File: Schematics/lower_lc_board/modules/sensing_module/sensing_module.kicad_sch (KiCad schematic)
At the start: 21 parts, among them J4 HALL-1, J5 HALL-2, Q3 2N7002, U11 SI2301CDS-T1-GE3, U9 ADC_ADS131M04IPWR

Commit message: organizational work
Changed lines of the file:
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@@
 	(text "place near sensor VCC pin"
 		(exclude_from_sim no)
-		(at 54.102 169.926 0)
+		(at 49.276 170.18 0)
 		(effects
 			(font

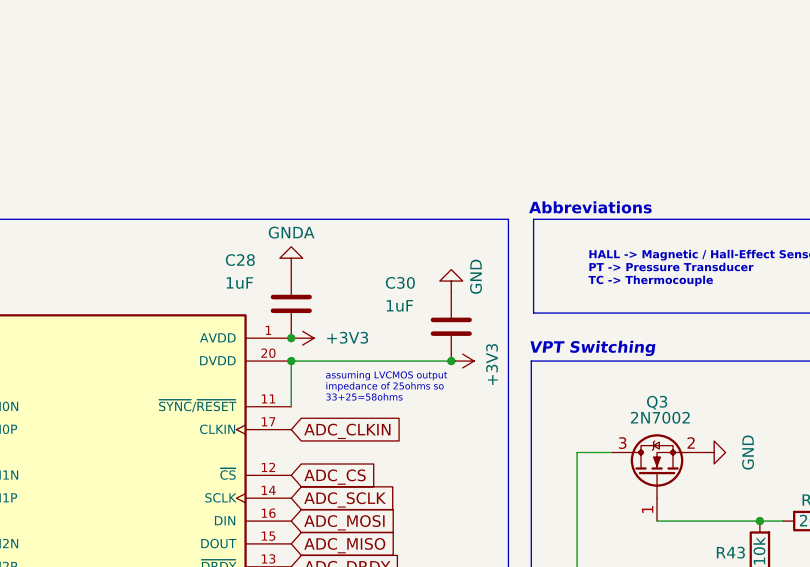
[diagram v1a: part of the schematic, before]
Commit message: more organizational work, add shared footprint, model, symbol dirs and clean up individuals
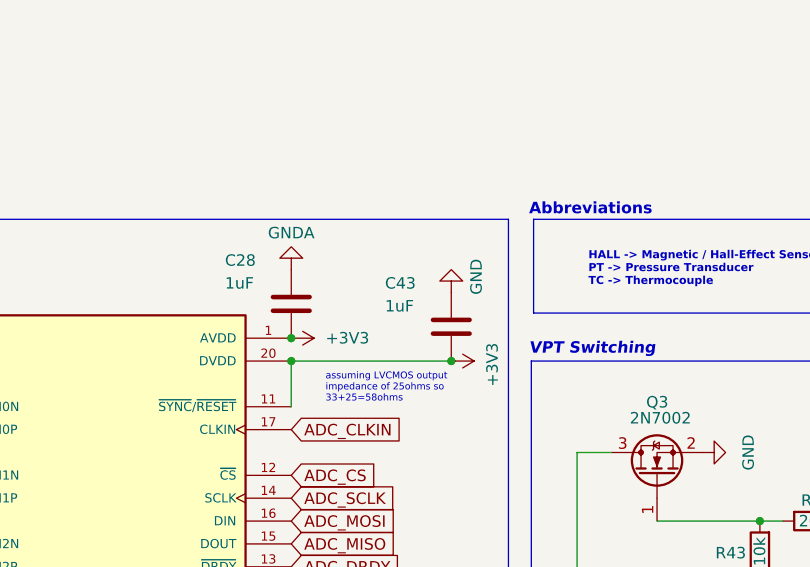
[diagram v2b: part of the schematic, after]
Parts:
- J4, J5: footprint S04B_PASK_2:CONN4_S04B-PASK_JST -> B04B_PASK_JST:CONN_B04B-PASK_JST
- renumbered C30 to C43
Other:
- title: Lower Board Sensing Module -> HYDRA | Sensing Circuitry
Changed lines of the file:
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@@
 	(paper "A4")
 	(title_block
-		(title "Lower Board Sensing Module")
-		(rev "B")
+		(title "HYDRA | Sensing Circuitry")
+		(rev "2")
 		(company "Queen's Rocket Engineering Team")
 		(comment 1 "Jeevan Sanchez")
@@
 			)
 		)
-		(property "Datasheet" "${KIPRJMOD}/../../Datasheets/NMOSFET-NDS7002A-D.PDF"
+		(property "Datasheet" "${KIPRJMOD}/../../Documentation/nmosfet_2N7002_DS.PDF"
 			(at 227.33 54.61 0)
 			(effects
@@
 			)
 		)
-		(property "Footprint" "S04B_PASK_2:CONN4_S04B-PASK_JST"
+		(property "Footprint" "B04B_PASK_JST:CONN_B04B-PASK_JST"
 			(at 49.53 154.94 0)
 			(effects
@@
 			)
 		)
-		(property "Datasheet" "${KIPRJMOD}/../../Datasheets/CONN-530470460.pdf"
+		(property "Datasheet" ""
 			(at 49.53 154.94 0)
 			(effects
@@
 		(on_board yes)
 		(dnp no)
-		(property "Reference" "C30"
+		(property "Reference" "C43"
 			(at 193.294 38.354 0)
 			(effects
@@
 			(project "lower_lc_board"
 				(path "/d63798c4-e363-437e-9012-e4aff32e6642/c6419db7-28a9-4bfa-8244-fc88166c795c"
-					(reference "C30")
+					(reference "C43")
 					(unit 1)
 				)
@@
 			)
 		)
-		(property "Datasheet" "https://www.vishay.com/doc?68741"
+		(property "Datasheet" "${KIPRJMOD}/../../Documentation/pmosfet_si2301cd_DS.pdf"
 			(at 229.87 80.01 0)
 			(effects
@@
 			)
 		)
-		(property "Footprint" "S04B_PASK_2:CONN4_S04B-PASK_JST"
+		(property "Footprint" "B04B_PASK_JST:CONN_B04B-PASK_JST"
 			(at 49.53 115.57 0)
 			(effects
@@
 			)
 		)
-		(property "Datasheet" "${KIPRJMOD}/../../Datasheets/CONN-530470460.pdf"
+		(property "Datasheet" ""
 			(at 49.53 115.57 0)
 			(effects
@@
 			)
 		)
-		(property "Datasheet" "${KIPRJMOD}/../../Datasheets/ADC-ads131m04.pdf"
+		(property "Datasheet" "${KIPRJMOD}/../../Documentation/ADC_ads131m04_DS.pdf"
 			(at 162.56 64.77 0)
 			(effects

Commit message: routing work
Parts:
- added R49: 10k, Resistor_SMD:R_0402_1005Metric, symbol Device:R
- C23, C33: JLCPCB (none) -> C49678
- J4, J5: footprint B04B_PASK_JST:CONN_B04B-PASK_JST -> S04B_PASK_2-P:CONN4_S04B-PASK_JST
- R22, R23: JLCPCB (none) -> C25744
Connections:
- net +3V3: now also R49.1
- net ADC_CS: now also R49.2
- net ADC_MISO renamed SPI_MISO
- net ADC_MOSI renamed SPI_MOSI
- net ADC_SCLK renamed SPI_SCLK
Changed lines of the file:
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@@
 		)
 	)
-	(global_label "ADC_DRDY"
+	(global_label "SPI_MISO"
 		(shape input)
-		(at 182.88 69.85 0)
+		(at 182.88 67.31 0)
 		(fields_autoplaced yes)
 		(effects
@@
 		)
 		(property "Intersheetrefs" "${INTERSHEET_REFS}"
-			(at 195.36 69.85 0)
+			(at 194.5133 67.31 0)
 			(effects
 				(font
@@
 		)
 	)
-	(global_label "HALL_SCL"
+	(global_label "ADC_DRDY"
 		(shape input)
-		(at 91.44 139.7 180)
+		(at 182.88 69.85 0)
 		(fields_autoplaced yes)
 		(effects
@@
 				(size 1.27 1.27)
 			)
-			(justify right)
+			(justify left)
 		)
 		(property "Intersheetrefs" "${INTERSHEET_REFS}"
-			(at 79.5043 139.7 0)
+			(at 195.36 69.85 0)
 			(effects
 				(font
 					(size 1.27 1.27)
 				)
-				(justify right)
+				(justify left)
 				(hide yes)
 			)
 		)
 	)
-	(global_label "ADC_CS"
+	(global_label "HALL_SCL"
 		(shape input)
-		(at 182.88 59.69 0)
+		(at 91.44 139.7 180)
 		(fields_autoplaced yes)
 		(effects
@@
 				(size 1.27 1.27)
 			)
-			(justify left)
+			(justify right)
 		)
 		(property "Intersheetrefs" "${INTERSHEET_REFS}"
-			(at 192.9409 59.69 0)
+			(at 79.5043 139.7 0)
 			(effects
 				(font
 					(size 1.27 1.27)
 				)
-				(justify left)
+				(justify right)
 				(hide yes)
 			)
 		)
 	)
-	(global_label "ADC_SCLK"
+	(global_label "ADC_CS"
 		(shape input)
-		(at 182.88 62.23 0)
+		(at 182.88 59.69 0)
 		(fields_autoplaced yes)
 		(effects
@@
 		)
 		(property "Intersheetrefs" "${INTERSHEET_REFS}"
-			(at 195.239 62.23 0)
+			(at 192.9409 59.69 0)
 			(effects
 				(font
@@
 		)
 	)
-	(global_label "ADC_MOSI"
+	(global_label "ADC_CLKIN"
 		(shape input)
-		(at 182.88 64.77 0)
+		(at 182.88 54.61 0)
 		(fields_autoplaced yes)
 		(effects
@@
 		)
 		(property "Intersheetrefs" "${INTERSHEET_REFS}"
-			(at 195.0576 64.77 0)
+			(at 195.9648 54.61 0)
 			(effects
 				(font
@@
 		)
 	)
-	(global_label "ADC_CLKIN"
+	(global_label "ADC_CS"
 		(shape input)
-		(at 182.88 54.61 0)
+		(at 203.2 78.74 90)
 		(fields_autoplaced yes)
 		(effects
@@
 		)
 		(property "Intersheetrefs" "${INTERSHEET_REFS}"
-			(at 195.9648 54.61 0)
+			(at 203.2 68.6791 90)
 			(effects
 				(font
@@
 		)
 	)
-	(global_label "ADC_MISO"
+	(global_label "SPI_SCLK"
 		(shape input)
-		(at 182.88 67.31 0)
+		(at 182.88 62.23 0)
 		(fields_autoplaced yes)
 		(effects
@@
 		)
 		(property "Intersheetrefs" "${INTERSHEET_REFS}"
-			(at 195.0576 67.31 0)
+			(at 194.6947 62.23 0)
 			(effects
 				(font
@@
 		)
 	)
+	(global_label "SPI_MOSI"
+		(shape input)
+		(at 182.88 64.77 0)
+		(fields_autoplaced yes)
+		(effects
+			(font
+				(size 1.27 1.27)
+			)
+			(justify left)
+		)
+		(property "Intersheetrefs" "${INTERSHEET_REFS}"
+			(at 194.5133 64.77 0)
+			(effects
+				(font
+					(size 1.27 1.27)
+				)
+				(justify left)
+				(hide yes)
+			)
+		)
+	)
 	(symbol
 		(lib_id "Device:C")
@@
 			)
 		)
+		(property "JLCPCB" "C25744"
+			(at 228.6 73.66 0)
+			(effects
+				(font
+					(size 1.27 1.27)
+				)
+				(hide yes)
+			)
+		)
 		(pin "1"
 		)
@@
 			)
 		)
+		(property "JLCPCB" "C49678"
+			(at 45.72 170.18 0)
+			(effects
+				(font
+					(size 1.27 1.27)
+				)
+				(hide yes)
+			)
+		)
 		(pin "2"
 		)
@@
 			)
 		)
-		(property "Footprint" "B04B_PASK_JST:CONN_B04B-PASK_JST"
+		(property "Footprint" "S04B_PASK_2-P:CONN4_S04B-PASK_JST"
 			(at 49.53 154.94 0)
 			(effects
@@
 			)
 		)
+		(property "JLCPCB" "C49678"
+			(at 45.72 130.81 0)
+			(effects
+				(font
+					(size 1.27 1.27)
+				)
+				(hide yes)
+			)
+		)
 		(pin "2"
 		)
@@
 	)
 	(symbol
+		(lib_id "power:+3V3")
+		(at 203.2 86.36 180)
+		(unit 1)
+		(exclude_from_sim no)
+		(in_bom yes)
+		(on_board yes)
+		(dnp no)
+		(property "Reference" "#PWR0132"
+			(at 203.2 82.55 0)
+			(effects
+				(font
+					(size 1.27 1.27)
+				)
+				(hide yes)
+			)
+		)
+		(property "Value" "+3V3"
+			(at 203.2 90.424 0)
+			(effects
+				(font
+					(size 1.27 1.27)
+				)
+			)
+		)
+		(property "Footprint" ""
+			(at 203.2 86.36 0)
+			(effects
+				(font
+					(size 1.27 1.27)
+				)
+				(hide yes)
+			)
+		)
+		(property "Datasheet" ""
+			(at 203.2 86.36 0)
+			(effects
+				(font
+					(size 1.27 1.27)
+				)
+				(hide yes)
+			)
+		)
+		(property "Description" "Power symbol creates a global label with name \"+3V3\""
+			(at 203.2 86.36 0)
+			(effects
+				(font
+					(size 1.27 1.27)
+				)
+				(hide yes)
+			)
+		)
+		(pin "1"
+		)
+		(instances
+			(project "lower_lc_board"
+				(path "/d63798c4-e363-437e-9012-e4aff32e6642/c6419db7-28a9-4bfa-8244-fc88166c795c"
+					(reference "#PWR0132")
+					(unit 1)
+				)
+			)
+		)
+	)
+	(symbol
 		(lib_id "Device:C")
 		(at 186.69 74.93 90)
@@
 			)
 		)
-		(property "Footprint" "B04B_PASK_JST:CONN_B04B-PASK_JST"
+		(property "Footprint" "S04B_PASK_2-P:CONN4_S04B-PASK_JST"
 			(at 49.53 115.57 0)
 			(effects
@@
 	(symbol
 		(lib_id "Device:R")
+		(at 203.2 82.55 180)
+		(unit 1)
+		(exclude_from_sim no)
+		(in_bom yes)
+		(on_board yes)
+		(dnp no)
+		(property "Reference" "R49"
+			(at 200.406 86.868 0)
+			(effects
+				(font
+					(size 1.27 1.27)
+				)
+				(justify left)
+			)
+		)
+		(property "Value" "10k"
+			(at 200.406 84.328 0)
+			(effects
+				(font
+					(size 1.27 1.27)
+				)
+				(justify left)
+			)
+		)
+		(property "Footprint" "Resistor_SMD:R_0402_1005Metric"
+			(at 204.978 82.55 90)
+			(effects
+				(font
+					(size 1.27 1.27)
+				)
+				(hide yes)
+			)
+		)
+		(property "Datasheet" "~"
+			(at 203.2 82.55 0)
+			(effects
+				(font
+					(size 1.27 1.27)
+				)
+				(hide yes)
+			)
+		)
+		(property "Description" "Resistor"
+			(at 203.2 82.55 0)
+			(effects
+				(font
+					(size 1.27 1.27)
+				)
+				(hide yes)
+			)
+		)
+		(property "JLCPCB" "C25744"
+			(at 203.2 82.55 0)
+			(effects
+				(font
+					(size 1.27 1.27)
+				)
+				(hide yes)
+			)
+		)
+		(pin "1"
+		)
+		(pin "2"
+		)
+		(instances
+			(project "lower_lc_board"
+				(path "/d63798c4-e363-437e-9012-e4aff32e6642/c6419db7-28a9-4bfa-8244-fc88166c795c"
+					(reference "R49")
+					(unit 1)
+				)
+			)
+		)
+	)
+	(symbol
+		(lib_id "Device:R")
 		(at 234.95 68.58 180)
 		(unit 1)
@@
 			(at 218.44 73.66 0)
 			(effects
+				(font
+					(size 1.27 1.27)
+				)
+				(hide yes)
+			)
+		)
+		(property "JLCPCB" "C25744"
+			(at 218.44 73.66 0)
+			(effects

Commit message: routing work
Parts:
- added C56: 10nF, Capacitor_SMD:C_0603_1608Metric, symbol Device:C
- added R25: 10k, Resistor_SMD:R_0603_1608Metric, symbol Device:R
- added TH1: Thermistor, Resistor_SMD:R_0402_1005Metric, symbol Device:Thermistor
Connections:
- net +3V3: now also R25.2
- net GNDA: now also TH1.2; no longer U9.10 (AIN3P), U9.9 (AIN3N)
- net TEMP_SENSE: now also R25.1, TH1.1
- net TC_N_CLAMPED renamed TC_N_CLAMPED_1
- net TC_P_CLAMPED renamed TC_P_CLAMPED_1
- new net TC_N_CLAMPED_2: C56.1, U9.9 (AIN3N)
- new net TC_P_CLAMPED_2: C56.2, U9.10 (AIN3P)
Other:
- added sheet TC Conditoning + CJC1 (../../../shared_schematics/TC_module.kicad_sch)
- sheet TC Conditoning + CJC ports: added none; removed TMP-OUT
- note added: "place as close as possible to thermocouple input for CJC measuring accuracy"

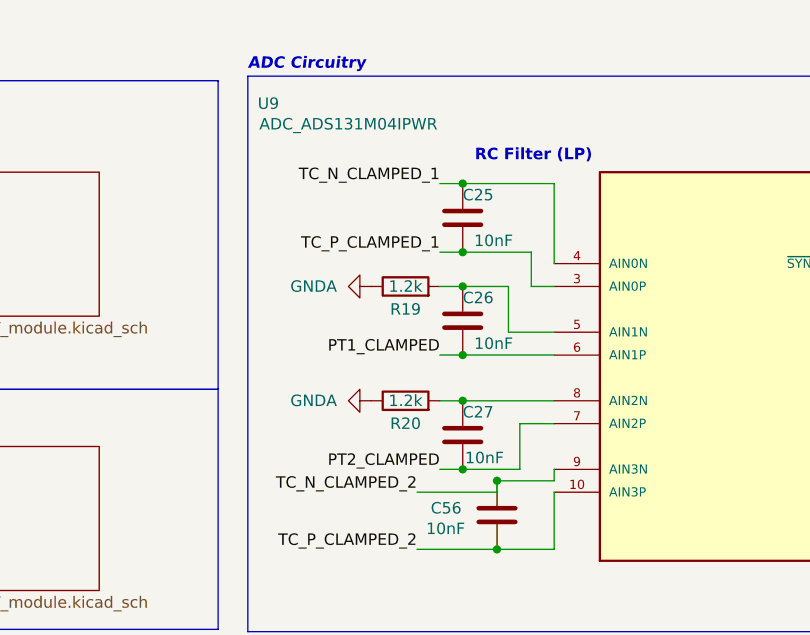
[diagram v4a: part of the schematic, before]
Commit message: ADC routing
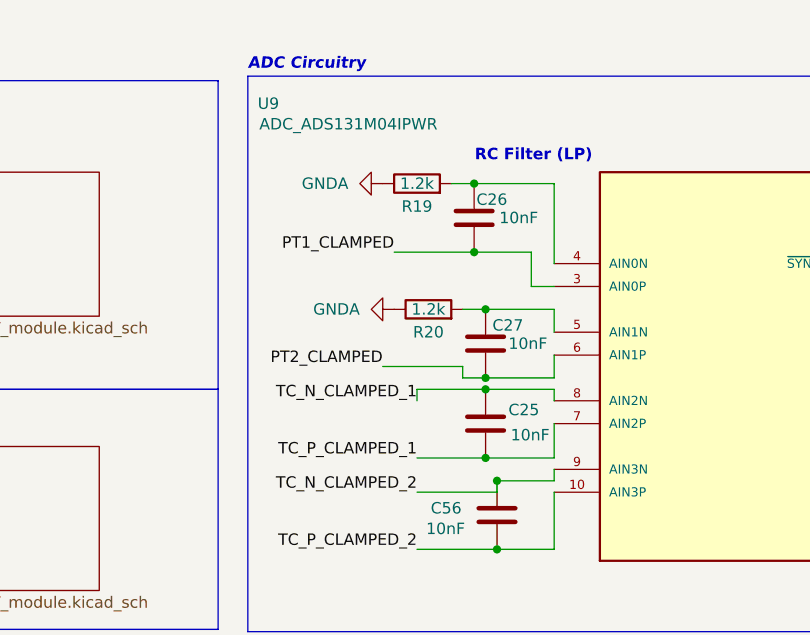
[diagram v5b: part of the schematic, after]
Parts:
- C29: footprint Capacitor_SMD:C_0805_2012Metric -> Capacitor_SMD:C_0402_1005Metric
- R19, R20: footprint Resistor_SMD:R_0603_1608Metric -> Resistor_SMD:R_0402_1005Metric
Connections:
- net PT1_CLAMPED: now also U9.3 (AIN0P); no longer U9.6 (AIN1P)
- net PT2_CLAMPED: now also U9.6 (AIN1P); no longer U9.7 (AIN2P)
- net TC_N_CLAMPED_1: now also U9.8 (AIN2N); no longer U9.4 (AIN0N)
- net TC_P_CLAMPED_1: now also U9.7 (AIN2P); no longer U9.3 (AIN0P)
- net at C26.1, R19.2: now also U9.4 (AIN0N); no longer U9.5 (AIN1N)
- net at C27.1, R20.2: now also U9.5 (AIN1N); no longer U9.8 (AIN2N)
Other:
- moved on the sheet: C25, C26, C27, R19, R20

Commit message: routing work
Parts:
- added C35: 10uF, Capacitor_SMD:C_1206_3216Metric, symbol Device:C
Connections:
- net GND: no longer Q3.2 (S), R43.1
- net GNDA: now also Q3.2 (S), R43.1, C35.2
- net VPT: now also C35.1
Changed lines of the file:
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@@
 	(wire
 		(pts
+			(xy 100.33 39.37) (xy 100.33 40.64)
+		)
+		(stroke
+			(width 0)
+			(type default)
+		)
+	)
+	(wire
+		(pts
 			(xy 223.52 116.84) (xy 223.52 118.11)
 		)
@@
 		)
 	)
+	(label "VPT"
+		(at 100.33 39.37 180)
+		(fields_autoplaced yes)
+		(effects
+			(font
+				(size 1.27 1.27)
+			)
+			(justify right bottom)
+		)
+	)
 	(label "PT1_CLAMPED"
 		(at 49.53 54.61 180)
@@
 	)
 	(symbol
-		(lib_id "power:GND")
-		(at 234.95 72.39 90)
-		(unit 1)
-		(exclude_from_sim no)
-		(in_bom yes)
-		(on_board yes)
-		(dnp no)
-		(fields_autoplaced yes)
-		(property "Reference" "#PWR0112"
-			(at 241.3 72.39 0)
-			(effects
-				(font
-					(size 1.27 1.27)
-				)
-				(hide yes)
-			)
-		)
-		(property "Value" "GND"
-			(at 240.03 72.39 0)
-			(effects
-				(font
-					(size 1.27 1.27)
-				)
-			)
-		)
-		(property "Footprint" ""
-			(at 234.95 72.39 0)
-			(effects
-				(font
-					(size 1.27 1.27)
-				)
-				(hide yes)
-			)
-		)
-		(property "Datasheet" ""
-			(at 234.95 72.39 0)
-			(effects
-				(font
-					(size 1.27 1.27)
-				)
-				(hide yes)
-			)
-		)
-		(property "Description" "Power symbol creates a global label with name \"GND\" , ground"
-			(at 234.95 72.39 0)
-			(effects
-				(font
-					(size 1.27 1.27)
-				)
-				(hide yes)
-			)
-		)
-		(pin "1"
-		)
-		(instances
-			(project "lower_lc_board"
-				(path "/d63798c4-e363-437e-9012-e4aff32e6642/c6419db7-28a9-4bfa-8244-fc88166c795c"
-					(reference "#PWR0112")
-					(unit 1)
-				)
-			)
-		)
-	)
-	(symbol
 		(lib_id "Connector_Generic:Conn_01x04")
 		(at 49.53 154.94 180)
@@
 	)
 	(symbol
+		(lib_id "power:GNDA")
+		(at 228.6 57.15 90)
+		(unit 1)
+		(exclude_from_sim no)
+		(in_bom yes)
+		(on_board yes)
+		(dnp no)
+		(fields_autoplaced yes)
+		(property "Reference" "#PWR088"
+			(at 234.95 57.15 0)
+			(effects
+				(font
+					(size 1.27 1.27)
+				)
+				(hide yes)
+			)
+		)
+		(property "Value" "GNDA"
+			(at 232.41 57.1499 90)
+			(effects
+				(font
+					(size 1.27 1.27)
+				)
+				(justify right)
+			)
+		)
+		(property "Footprint" ""
+			(at 228.6 57.15 0)
+			(effects
+				(font
+					(size 1.27 1.27)
+				)
+				(hide yes)
+			)
+		)
+		(property "Datasheet" ""
+			(at 228.6 57.15 0)
+			(effects
+				(font
+					(size 1.27 1.27)
+				)
+				(hide yes)
+			)
+		)
+		(property "Description" "Power symbol creates a global label with name \"GNDA\" , analog ground"
+			(at 228.6 57.15 0)
+			(effects
+				(font
+					(size 1.27 1.27)
+				)
+				(hide yes)
+			)
+		)
+		(pin "1"
+		)
+		(instances
+			(project "lower_lc_board"
+				(path "/d63798c4-e363-437e-9012-e4aff32e6642/c6419db7-28a9-4bfa-8244-fc88166c795c"
+					(reference "#PWR088")
+					(unit 1)
+				)
+			)
+		)
+	)
+	(symbol
 		(lib_id "power:+3V3")
 		(at 91.44 148.59 180)
@@
 	)
 	(symbol
+		(lib_id "power:GNDA")
+		(at 234.95 72.39 90)
+		(unit 1)
+		(exclude_from_sim no)
+		(in_bom yes)
+		(on_board yes)
+		(dnp no)
+		(fields_autoplaced yes)
+		(property "Reference" "#PWR0112"
+			(at 241.3 72.39 0)
+			(effects
+				(font
+					(size 1.27 1.27)
+				)
+				(hide yes)
+			)
+		)
+		(property "Value" "GNDA"
+			(at 238.76 72.3899 90)
+			(effects
+				(font
+					(size 1.27 1.27)
+				)
+				(justify right)
+			)
+		)
+		(property "Footprint" ""
+			(at 234.95 72.39 0)
+			(effects
+				(font
+					(size 1.27 1.27)
+				)
+				(hide yes)
+			)
+		)
+		(property "Datasheet" ""
+			(at 234.95 72.39 0)
+			(effects
+				(font
+					(size 1.27 1.27)
+				)
+				(hide yes)
+			)
+		)
+		(property "Description" "Power symbol creates a global label with name \"GNDA\" , analog ground"
+			(at 234.95 72.39 0)
+			(effects
+				(font
+					(size 1.27 1.27)
+				)
+				(hide yes)
+			)
+		)
+		(pin "1"
+		)
+		(instances
+			(project "lower_lc_board"
+				(path "/d63798c4-e363-437e-9012-e4aff32e6642/c6419db7-28a9-4bfa-8244-fc88166c795c"
+					(reference "#PWR0112")
+					(unit 1)
+				)
+			)
+		)
+	)
+	(symbol
 		(lib_id "power:+3V3")
 		(at 91.44 132.08 180)
@@
 	)
 	(symbol
-		(lib_id "power:GND")
-		(at 228.6 57.15 90)
-		(unit 1)
-		(exclude_from_sim no)
-		(in_bom yes)
-		(on_board yes)
-		(dnp no)
-		(fields_autoplaced yes)
-		(property "Reference" "#PWR088"
-			(at 234.95 57.15 0)
-			(effects
-				(font
-					(size 1.27 1.27)
-				)
-				(hide yes)
-			)
-		)
-		(property "Value" "GND"
-			(at 233.68 57.15 0)
-			(effects
-				(font
-					(size 1.27 1.27)
-				)
-			)
-		)
-		(property "Footprint" ""
-			(at 228.6 57.15 0)
-			(effects
-				(font
-					(size 1.27 1.27)
-				)
-				(hide yes)
-			)
-		)
-		(property "Datasheet" ""
-			(at 228.6 57.15 0)
-			(effects
-				(font
-					(size 1.27 1.27)
-				)
-				(hide yes)
-			)
-		)
-		(property "Description" "Power symbol creates a global label with name \"GND\" , ground"
-			(at 228.6 57.15 0)
-			(effects
-				(font
-					(size 1.27 1.27)
-				)
-				(hide yes)
-			)
-		)
-		(pin "1"
-		)
-		(instances
-			(project ""
-				(path "/d63798c4-e363-437e-9012-e4aff32e6642/c6419db7-28a9-4bfa-8244-fc88166c795c"
-					(reference "#PWR088")
-					(unit 1)
-				)
-			)
-		)
-	)
-	(symbol
 		(lib_id "Device:R")
 		(at 203.2 82.55 180)
@@
 	)
 	(symbol
+		(lib_id "Device:C")
+		(at 100.33 44.45 0)
+		(unit 1)
+		(exclude_from_sim no)
+		(in_bom yes)
+		(on_board yes)
+		(dnp no)
+		(property "Reference" "C35"
+			(at 92.964 43.434 0)
+			(effects
+				(font
+					(size 1.27 1.27)
+				)
+				(justify left)
+			)
+		)
+		(property "Value" "10uF"
+			(at 92.964 45.974 0)
+			(effects
+				(font
+					(size 1.27 1.27)
+				)
+				(justify left)
+			)
+		)
+		(property "Footprint" "Capacitor_SMD:C_1206_3216Metric"
+			(at 101.2952 48.26 0)
+			(effects
+				(font
+					(size 1.27 1.27)
+				)
+				(hide yes)
+			)
+		)
+		(property "Datasheet" "~"
+			(at 100.33 44.45 0)
+			(effects
+				(font
+					(size 1.27 1.27)
+				)
+				(hide yes)
+			)
+		)
+		(property "Description" "Unpolarized capacitor"
+			(at 100.33 44.45 0)
+			(effects
+				(font
+					(size 1.27 1.27)
+				)
+				(hide yes)
+			)
+		)
+		(pin "2"
+		)
+		(pin "1"
+		)
+		(instances
+			(project "lower_lc_board"
+				(path "/d63798c4-e363-437e-9012-e4aff32e6642/c6419db7-28a9-4bfa-8244-fc88166c795c"
+					(reference "C35")
+					(unit 1)
+				)
+			)
+		)
+	)
+	(symbol
 		(lib_id "ADS131M04:ADS131M04IPWR")
 		(at 162.56 64.77 0)
@@
 					(unit 1)
 				)
+			)
+		)
+	)
+	(symbol
+		(lib_id "power:GNDA")
+		(at 100.33 48.26 0)
+		(unit 1)
+		(exclude_from_sim no)
+		(in_bom yes)
+		(on_board yes)
+		(dnp no)
+		(fields_autoplaced yes)
+		(property "Reference" "#PWR065"
+			(at 100.33 54.61 0)
+			(effects
+				(font
+					(size 1.27 1.27)
+				)
+				(hide yes)
+			)
+		)
+		(property "Value" "GNDA"
+			(at 100.33 53.34 0)
+			(effects
+				(font
+					(size 1.27 1.27)
+				)
+			)
+		)
+		(property "Footprint" ""
+			(at 100.33 48.26 0)
+			(effects
+				(font
+					(size 1.27 1.27)
+				)
+				(hide yes)
+			)
+		)
+		(property "Datasheet" ""
+			(at 100.33 48.26 0)
+			(effects
+				(font
+					(size 1.27 1.27)
+				)
+				(hide yes)
+			)
+		)
+		(property "Description" "Power symbol creates a global label with name \"GNDA\" , analog ground"
+			(at 100.33 48.26 0)
+			(effects
+				(font
+					(size 1.27 1.27)
+				)
+				(hide yes)
+			)
+		)
+		(pin "1"
+		)
+		(instances
+			(project "lower_lc_board"
+				(path "/d63798c4-e363-437e-9012-e4aff32e6642/c6419db7-28a9-4bfa-8244-fc88166c795c"
+					(reference "#PWR065")
+					(unit 1)
+				)

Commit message: analog routing, start 3V3 power routing
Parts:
- R17, R18: footprint Resistor_SMD:R_0603_1608Metric -> Resistor_SMD:R_0402_1005Metric
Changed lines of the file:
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@@
 			)
 		)
-		(property "Footprint" "Resistor_SMD:R_0603_1608Metric"
+		(property "Footprint" "Resistor_SMD:R_0402_1005Metric"
 			(at 89.662 128.27 90)
 			(effects
@@
 			)
 		)
-		(property "Footprint" "Resistor_SMD:R_0603_1608Metric"
+		(property "Footprint" "Resistor_SMD:R_0402_1005Metric"
 			(at 93.218 144.78 90)
 			(effects
